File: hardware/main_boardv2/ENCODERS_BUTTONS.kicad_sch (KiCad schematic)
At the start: 5 parts, among them J601 2x5 Socket Pins, J602 Conn_01x05_Pin, J603 Conn_01x05_Pin

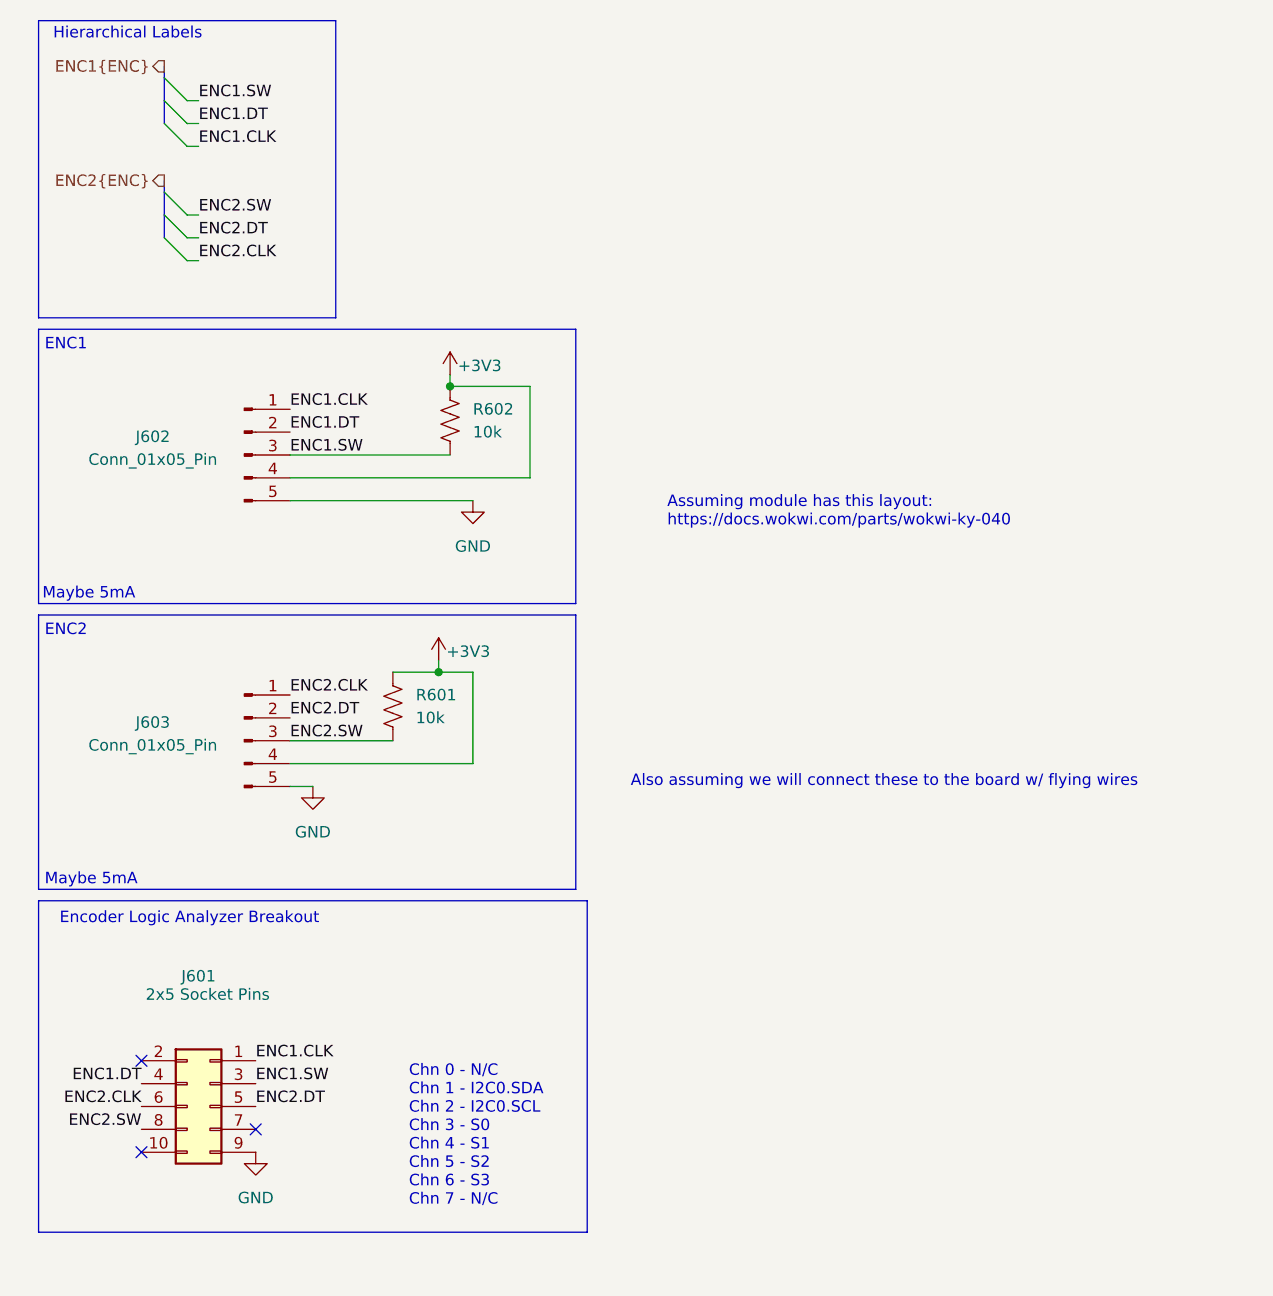
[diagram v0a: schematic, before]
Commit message: schematic sorta done? resized all RC packages to 0805
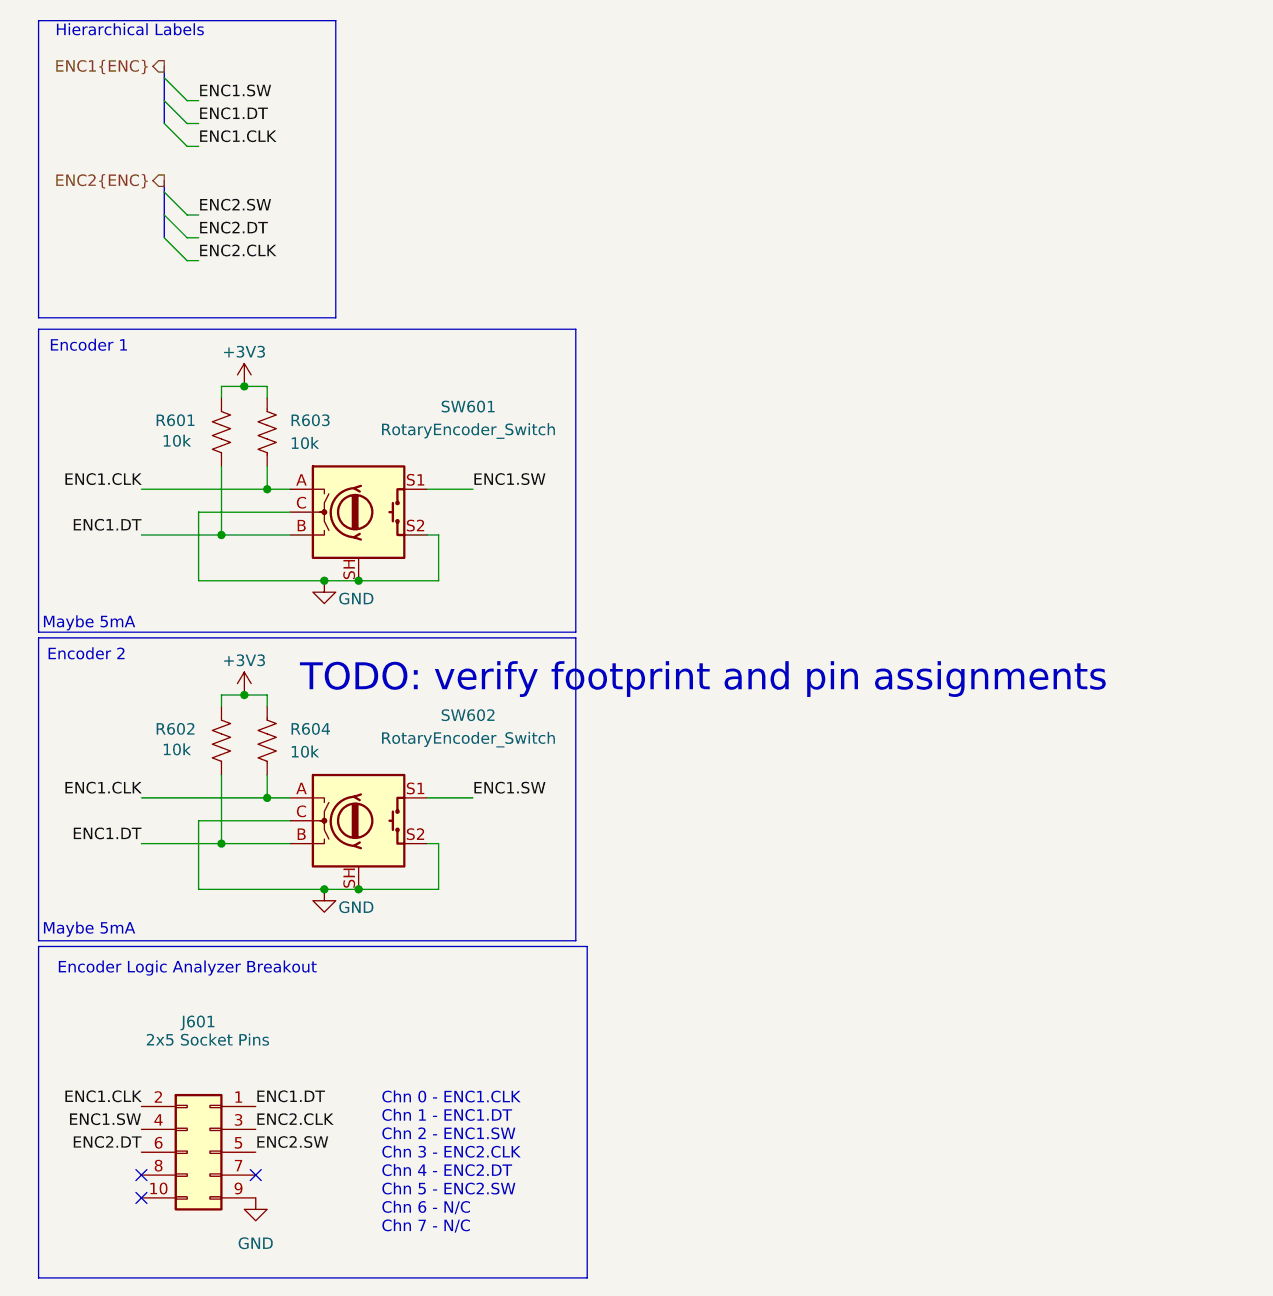
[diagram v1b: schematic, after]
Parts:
- removed J602, J603: Conn_01x05_Pin, Connector_PinHeader_2.54mm:PinHeader_1x05_P2.54mm_Vertical, symbol Connector:Conn_01x05_Pin
- added R602, R604: 10k, Resistor_SMD:R_0805_2012Metric, symbol Device:R_US
- added SW601, SW602: RotaryEncoder_Switch, Rotary_Encoder:RotaryEncoder_Bourns_Vertical_PEC12R-3x17F-Sxxxx, symbol SamacSys_Parts:shield_rotaryencoder
- renumbered R602 to R603
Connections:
- net +3V3: now also R602.2, R604.2
- net ENC1.CLK: now also J601.2 (Pin_2), R603.1, R604.1, SW601.A, SW602.A; no longer J601.1 (Pin_1)
- net ENC1.DT: now also J601.1 (Pin_1), R601.1, R602.1, SW601.B, SW602.B; no longer J601.4 (Pin_4)
- net ENC1.SW: now also J601.4 (Pin_4), SW601.S1, SW602.S1; no longer J601.3 (Pin_3), R603.1
- net ENC2.CLK: now also J601.3 (Pin_3); no longer J601.6 (Pin_6)
- net ENC2.DT: now also J601.6 (Pin_6); no longer J601.5 (Pin_5)
- net ENC2.SW: now also J601.5 (Pin_5); no longer J601.8 (Pin_8), R601.1
- net GND: now also SW601.C, SW601.S2, SW601.SH, SW602.C, SW602.S2, SW602.SH
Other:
- note added: "Chn 0 - ENC1.CLK Chn 1 - ENC1.DT Chn 2 - ENC1.SW Chn 3 - ENC2.CLK Chn 4 - ENC2.DT Chn 5 - ENC2.SW Chn 6 - N/C Chn 7 - N/C"
- note added: "Encoder 1"
- note added: "Encoder 2"
- note added: "TODO: verify footprint and pin assignments"
- note removed: "Also assuming we will connect these to the board w/ flying wires"
- note removed: "Assuming module has this layout: https://docs.wokwi.com/parts/wokwi-ky-040"
- note removed: "Chn 0 - N/C Chn 1 - I2C0.SDA Chn 2 - I2C0.SCL Chn 3 - S0 Chn 4 - S1 Chn 5 - S2 Chn 6 - S3 Chn 7 - N/C"
- note removed: "ENC1"
- note removed: "ENC2"
- moved on the sheet: J601, R603

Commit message: resized all package to 0603
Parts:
- R601, R602, R603, R604: footprint Resistor_SMD:R_0805_2012Metric -> Resistor_SMD:R_0603_1608Metric; Mouser Price/Stock https://www.mouser.com/ProductDetail/YAGEO/RV0805JR-0710KL?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 -> (none)
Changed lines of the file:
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@@
 			)
 		)
-		(property "Footprint" "Resistor_SMD:R_0805_2012Metric"
+		(property "Footprint" "Resistor_SMD:R_0603_1608Metric"
 			(at 34.798 59.69 90)
 			(effects
@@
 			)
 		)
-		(property "Mouser Price/Stock" "https://www.mouser.com/ProductDetail/YAGEO/RV0805JR-0710KL?qs=qpJ%252B%252B%252Bdg6p3bGiIDT3p%252B0w%3D%3D"
+		(property "Mouser Price/Stock" ""
 			(at 33.02 59.69 0)
 			(effects
@@
 			)
 		)
-		(property "Footprint" "Resistor_SMD:R_0805_2012Metric"
+		(property "Footprint" "Resistor_SMD:R_0603_1608Metric"
 			(at 39.878 59.69 90)
 			(effects
@@
 			)
 		)
-		(property "Mouser Price/Stock" "https://www.mouser.com/ProductDetail/YAGEO/RV0805JR-0710KL?qs=qpJ%252B%252B%252Bdg6p3bGiIDT3p%252B0w%3D%3D"
+		(property "Mouser Price/Stock" ""
 			(at 38.1 59.69 0)
 			(effects
@@
 			)
 		)
-		(property "Footprint" "Resistor_SMD:R_0805_2012Metric"
+		(property "Footprint" "Resistor_SMD:R_0603_1608Metric"
 			(at 34.798 93.98 90)
 			(effects
@@
 			)
 		)
-		(property "Mouser Price/Stock" "https://www.mouser.com/ProductDetail/YAGEO/RV0805JR-0710KL?qs=qpJ%252B%252B%252Bdg6p3bGiIDT3p%252B0w%3D%3D"
+		(property "Mouser Price/Stock" ""
 			(at 33.02 93.98 0)
 			(effects
@@
 			)
 		)
-		(property "Footprint" "Resistor_SMD:R_0805_2012Metric"
+		(property "Footprint" "Resistor_SMD:R_0603_1608Metric"
 			(at 39.878 93.98 90)
 			(effects
@@
 			)
 		)
-		(property "Mouser Price/Stock" "https://www.mouser.com/ProductDetail/YAGEO/RV0805JR-0710KL?qs=qpJ%252B%252B%252Bdg6p3bGiIDT3p%252B0w%3D%3D"
+		(property "Mouser Price/Stock" ""
 			(at 38.1 93.98 0)
 			(effects
